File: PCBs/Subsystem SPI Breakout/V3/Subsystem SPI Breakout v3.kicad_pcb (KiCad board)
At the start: 2 copper layers, 91.4 x 53.3 mm, 33 parts

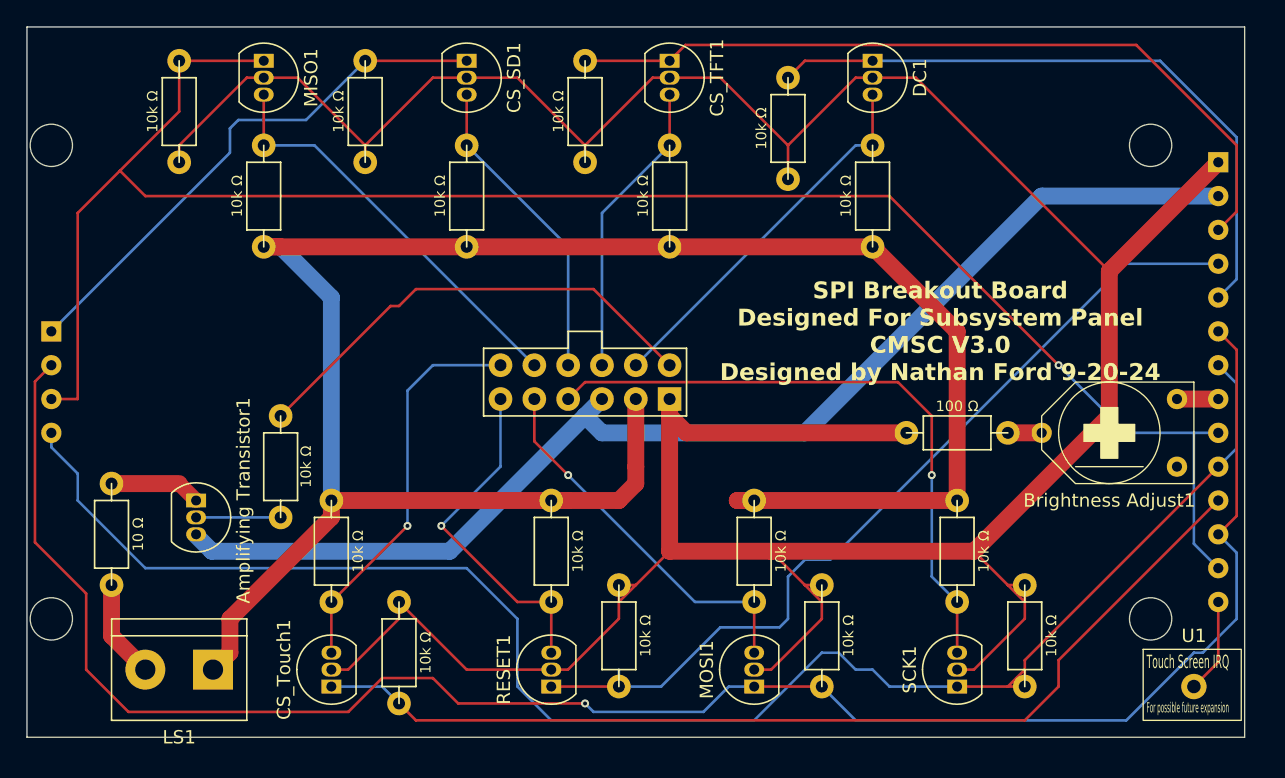
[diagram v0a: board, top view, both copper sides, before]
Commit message: Fixed drill hole positions
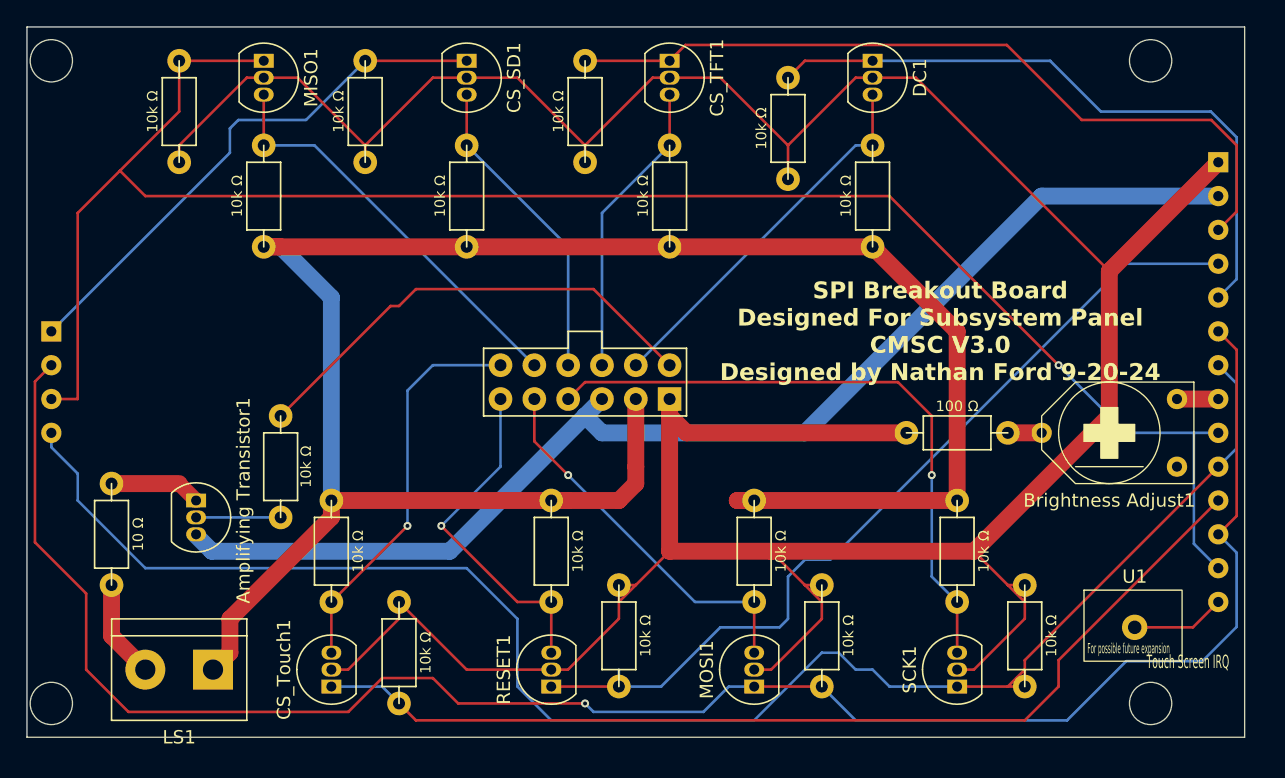
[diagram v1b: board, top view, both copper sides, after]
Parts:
- moved U1 6.29 mm to (189.9, 113.7)
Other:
- board text added: "Touch Screen IRQ"
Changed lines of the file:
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@@
 	(footprint "Subsystem Main Extra Symbols:T_IRQ"
 		(layer "F.Cu")
-		(at 194.31 118.11)
+		(at 189.865 113.665)
 		(property "Reference" "U1"
 			(at 0 -3.81 0)
@@
 			(layer "F.SilkS")
 		)
-		(fp_text user "Touch Screen IRQ"
-			(at -3.556 -1.27 0)
-			(unlocked yes)
-			(layer "F.SilkS")
-			(effects
-				(font
-					(size 1 0.508)
-					(thickness 0.1)
-				)
-				(justify left bottom)
-			)
-		)
 		(fp_text user "For possible future expansion"
 			(at -3.556 2.032 0)
@@
 		)
 		(pad "" np_thru_hole circle
-			(at 7.62 -17.78 180)
+			(at 7.62 -24.13 180)
 			(size 2.794 2.794)
 			(drill 3.175)
@@
 		)
 		(pad "" np_thru_hole circle
-			(at 7.62 17.78 180)
+			(at 7.62 24.13 180)
 			(size 2.794 2.794)
 			(drill 3.175)
@@
 		)
 		(pad "" np_thru_hole circle
-			(at 90.17 -17.78 180)
+			(at 90.17 -24.13 180)
 			(size 2.794 2.794)
 			(drill 3.175)
@@
 		)
 		(pad "" np_thru_hole circle
-			(at 90.17 17.78 180)
+			(at 90.17 24.13 180)
 			(size 2.794 2.794)
 			(drill 3.175)
@@
 		(layer "Edge.Cuts")
 	)
+	(gr_text "Touch Screen IRQ"
+		(at 190.754 116.84 0)
+		(layer "F.SilkS")
+		(effects
+			(font
+				(size 1 0.508)
+				(thickness 0.1)
+			)
+			(justify left bottom)
+		)
+	)
 	(gr_text "SPI Breakout Board\nDesigned For Subsystem Panel\nCMSC V3.0\nDesigned by Nathan Ford 9-20-24"
 		(at 175.26 95.25 0)
@@
 	)
 	(segment
-		(start 157.48 120.015)
-		(end 149.225 120.015)
+		(start 189.23 116.205)
+		(end 184.785 120.65)
 		(width 0.2)
 		(layer "B.Cu")
@@
 	)
 	(segment
-		(start 197.52 113.03)
-		(end 194.98 115.57)
+		(start 157.48 120.015)
+		(end 149.225 120.015)
 		(width 0.2)
 		(layer "B.Cu")
@@
 	)
 	(segment
-		(start 189.23 120.65)
-		(end 168.91 120.65)
+		(start 197.52 113.63)
+		(end 194.945 116.205)
 		(width 0.2)
 		(layer "B.Cu")
@@
 	)
 	(segment
-		(start 197.52 108.06)
-		(end 197.52 113.03)
+		(start 168.91 120.65)
+		(end 166.37 118.11)
 		(width 0.2)
 		(layer "B.Cu")
@@
 	)
 	(segment
-		(start 194.98 115.57)
-		(end 194.31 115.57)
+		(start 196.14 106.68)
+		(end 197.52 108.06)
 		(width 0.2)
 		(layer "B.Cu")
@@
 	)
 	(segment
-		(start 196.14 106.68)
-		(end 197.52 108.06)
+		(start 194.945 116.205)
+		(end 189.23 116.205)
 		(width 0.2)
 		(layer "B.Cu")
@@
 	)
 	(segment
-		(start 194.31 115.57)
-		(end 189.23 120.65)
+		(start 184.785 120.65)
+		(end 168.91 120.65)
 		(width 0.2)
 		(layer "B.Cu")
@@
 	)
 	(segment
-		(start 168.91 120.65)
-		(end 166.37 118.11)
+		(start 197.52 108.06)
+		(end 197.52 113.63)
 		(width 0.2)
 		(layer "B.Cu")
@@
 	)
 	(segment
-		(start 197.52 77.47)
-		(end 189.981 69.931)
+		(start 185.893 75.565)
+		(end 195.615 75.565)
 		(width 0.2)
 		(layer "F.Cu")
@@
 	)
 	(segment
-		(start 156.129 69.931)
-		(end 154.94 71.12)
+		(start 180.259 69.931)
+		(end 185.893 75.565)
 		(width 0.2)
 		(layer "F.Cu")
@@
 	)
 	(segment
-		(start 148.59 71.12)
-		(end 154.94 71.12)
+		(start 197.52 77.47)
+		(end 197.52 82.44)
 		(width 0.2)
 		(layer "F.Cu")
@@
 	)
 	(segment
-		(start 189.981 69.931)
+		(start 197.52 82.44)
+		(end 196.14 83.82)
+		(width 0.2)
+		(layer "F.Cu")
+		(net 16)
+	)
+	(segment
+		(start 154.94 71.12)
 		(end 156.129 69.931)
 		(width 0.2)
@@
 	)
 	(segment
-		(start 197.52 82.44)
-		(end 197.52 77.47)
+		(start 156.129 69.931)
+		(end 180.259 69.931)
 		(width 0.2)
 		(layer "F.Cu")
@@
 	)
 	(segment
-		(start 196.14 83.82)
-		(end 197.52 82.44)
+		(start 148.59 71.12)
+		(end 154.94 71.12)
+		(width 0.2)
+		(layer "F.Cu")
+		(net 16)
+	)
+	(segment
+		(start 195.615 75.565)
+		(end 197.52 77.47)
 		(width 0.2)
 		(layer "F.Cu")
@@
 	)
 	(segment
+		(start 197.52 87.52)
+		(end 197.52 76.87)
+		(width 0.2)
+		(layer "B.Cu")
+		(net 17)
+	)
+	(segment
 		(start 197.52 76.87)
-		(end 191.77 71.12)
+		(end 195.58 74.93)
 		(width 0.2)
 		(layer "B.Cu")
@@
 	)
 	(segment
-		(start 197.52 87.52)
-		(end 197.52 76.87)
+		(start 183.515 71.12)
+		(end 170.18 71.12)
 		(width 0.2)
 		(layer "B.Cu")
@@
 	)
 	(segment
-		(start 196.14 88.9)
-		(end 197.52 87.52)
+		(start 187.325 74.93)
+		(end 183.515 71.12)
 		(width 0.2)
 		(layer "B.Cu")
@@
 	)
 	(segment
-		(start 191.77 71.12)
-		(end 170.18 71.12)
+		(start 195.58 74.93)
+		(end 187.325 74.93)
+		(width 0.2)
+		(layer "B.Cu")
+		(net 17)
+	)
+	(segment
+		(start 196.14 88.9)
+		(end 197.52 87.52)
 		(width 0.2)
 		(layer "B.Cu")
@@
 	)
 	(segment
-		(start 196.14 111.76)
-		(end 196.14 116.28)
+		(start 189.865 113.665)
+		(end 194.235 113.665)
 		(width 0.2)
 		(layer "F.Cu")
@@
 	)
 	(segment
-		(start 196.14 116.28)
-		(end 194.31 118.11)
+		(start 194.235 113.665)
+		(end 196.14 111.76)
 		(width 0.2)
 		(layer "F.Cu")
